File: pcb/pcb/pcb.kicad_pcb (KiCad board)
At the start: 2 copper layers, 58.4 x 44.4 mm, 27 parts, among them J1 UART, J2 Barrel_Jack, J3 Stepper, SW1 RESET, SW2 FLASH, U1 ESP32-WROOM-32, U2 TSR_1-2433

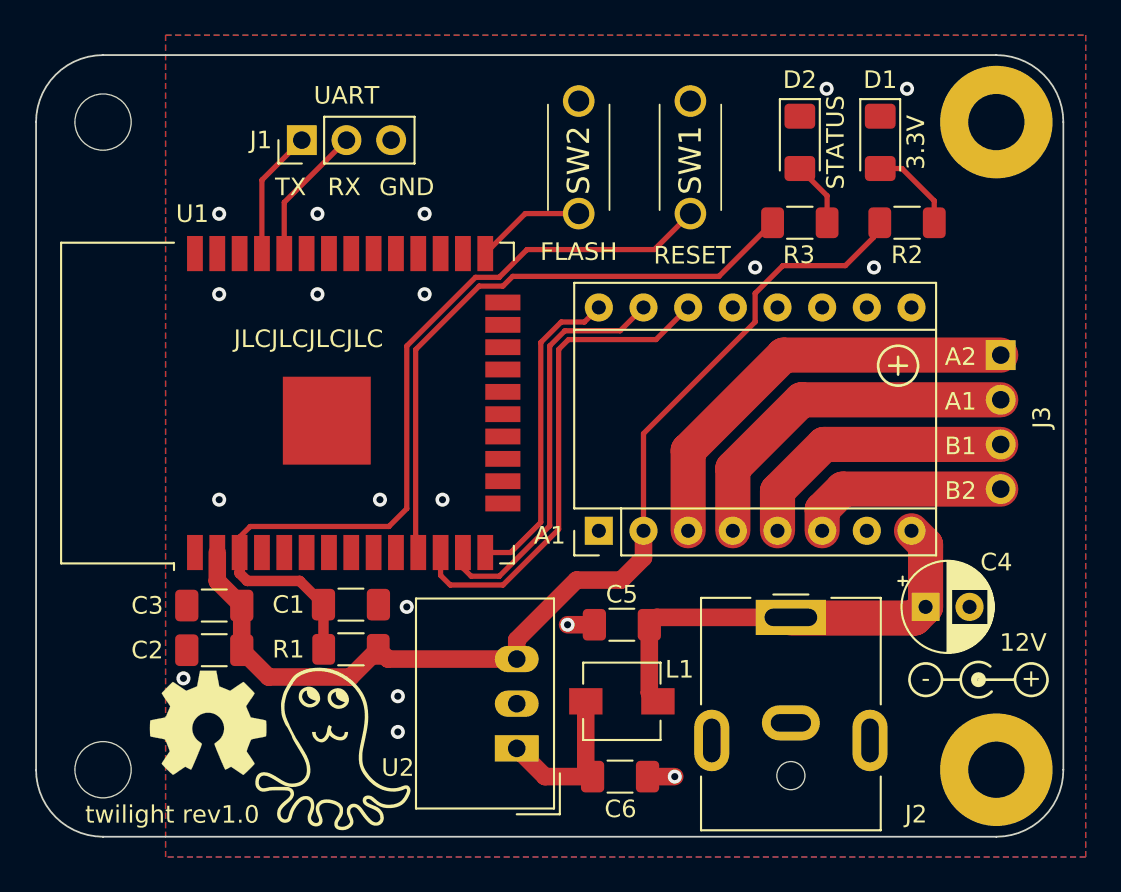
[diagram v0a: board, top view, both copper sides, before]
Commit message: Update pcb to fix bugs
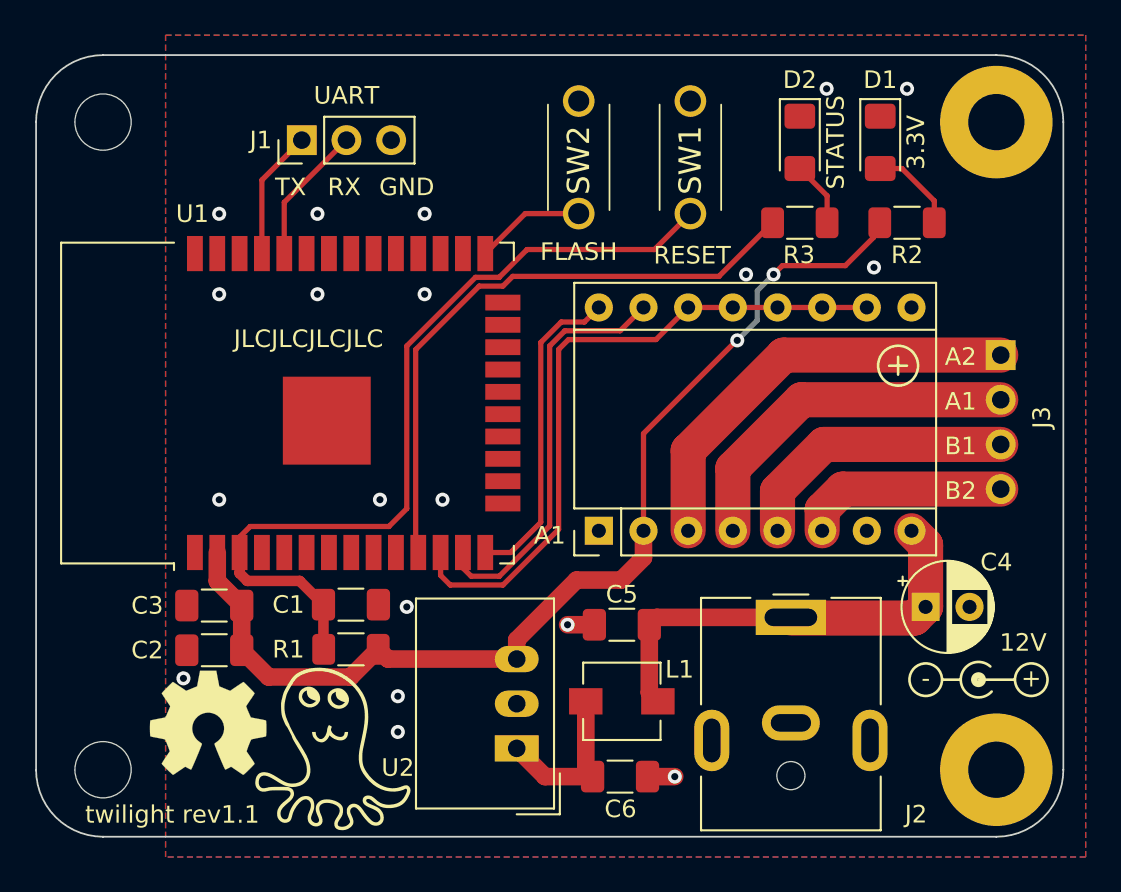
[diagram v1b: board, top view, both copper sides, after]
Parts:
- R2, R3: value 650 -> 680
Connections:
- A1 pad 10: unconnected-(A1-Pad10) -> /SLP
- A1 pad 11: unconnected-(A1-Pad11) -> /SLP
- A1 pad 12: unconnected-(A1-Pad12) -> /SLP
- A1 pad 13: unconnected-(A1-Pad13) -> /SLP
- U1 pad 39: (no net) -> GND
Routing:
- net /SLP: track 28.1 -> 38.3 mm
- net +3V3: track 59.7 -> 59.8 mm, vias 0 -> 2
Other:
- board text added: "twilight rev1.1"
- board text removed: "twilight rev1.0"

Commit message: Optimise routing
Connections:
- A1 pad 10: /SLP -> +3V3
- A1 pad 11: /SLP -> +3V3
- A1 pad 12: /SLP -> +3V3
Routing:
- net /SLP: track 38.3 -> 30.7 mm
- net +3V3: track 59.8 -> 66.2 mm, vias 2 -> 0
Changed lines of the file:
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@@
       (net 4 "unconnected-(A1-Pad9)") (pinfunction "~{EN}") (pintype "input"))
     (pad "10" thru_hole oval (at 12.7 15.24 90) (size 1.6 1.6) (drill 0.8) (layers *.Cu *.Mask)
-      (net 9 "/SLP") (pinfunction "M0") (pintype "input"))
+      (net 3 "+3V3") (pinfunction "M0") (pintype "input"))
     (pad "11" thru_hole oval (at 12.7 12.7 90) (size 1.6 1.6) (drill 0.8) (layers *.Cu *.Mask)
-      (net 9 "/SLP") (pinfunction "M1") (pintype "input"))
+      (net 3 "+3V3") (pinfunction "M1") (pintype "input"))
     (pad "12" thru_hole oval (at 12.7 10.16 90) (size 1.6 1.6) (drill 0.8) (layers *.Cu *.Mask)
-      (net 9 "/SLP") (pinfunction "M2") (pintype "input"))
+      (net 3 "+3V3") (pinfunction "M2") (pintype "input"))
     (pad "13" thru_hole oval (at 12.7 7.62 90) (size 1.6 1.6) (drill 0.8) (layers *.Cu *.Mask)
       (net 9 "/SLP") (pinfunction "~{RST}") (pintype "input"))
@@
   (segment (start 110.744 73.66) (end 108.204 73.66) (width 1) (layer "F.Cu") (net 3))
   (segment (start 90.69082 79.17152) (end 89.1671 77.6478) (width 1) (layer "F.Cu") (net 3))
+  (segment (start 118.596 57.528) (end 118.596 56.778) (width 0.3) (layer "F.Cu") (net 3))
+  (segment (start 118.346 59.236) (end 119.426 58.156) (width 0.3) (layer "F.Cu") (net 3))
   (segment (start 89.1671 77.6478) (end 89.1671 75.1078) (width 1) (layer "F.Cu") (net 3))
-  (segment (start 123.4948 55.7784) (end 125.096786 54.176414) (width 0.3) (layer "F.Cu") (net 3))
   (segment (start 96.927 77.597) (end 97.4799 78.1499) (width 1) (layer "F.Cu") (net 3))
-  (segment (start 125.096786 54.176414) (end 125.096786 53.693213) (width 0.3) (layer "F.Cu") (net 3))
-  (segment (start 117.346 60.028) (end 117.3148 60.028) (width 0.3) (layer "F.Cu") (net 3))
-  (segment (start 117.3148 60.028) (end 112.014 65.3288) (width 0.3) (layer "F.Cu") (net 3))
+  (segment (start 119.426 58.156) (end 119.634 58.156) (width 0.3) (layer "F.Cu") (net 3))
+  (segment (start 119.634 58.156) (end 119.224 58.156) (width 0.3) (layer "F.Cu") (net 3))
+  (segment (start 118.346 60.028) (end 118.346 59.236) (width 0.3) (layer "F.Cu") (net 3))
+  (segment (start 112.014 66.36) (end 118.346 60.028) (width 0.3) (layer "F.Cu") (net 3))
   (segment (start 104.8065 77.0575) (end 104.8065 78.1499) (width 1) (layer "F.Cu") (net 3))
-  (segment (start 119.909762 55.7784) (end 123.4948 55.7784) (width 0.3) (layer "F.Cu") (net 3))
   (segment (start 87.7754 73.7161) (end 87.7754 72.0922) (width 1) (layer "F.Cu") (net 3))
+  (segment (start 118.596 56.778) (end 119.5956 55.7784) (width 0.3) (layer "F.Cu") (net 3))
   (segment (start 96.927 77.597) (end 95.35248 79.17152) (width 1) (layer "F.Cu") (net 3))
+  (segment (start 122.174 58.156) (end 124.714 58.156) (width 0.3) (layer "F.Cu") (net 3))
   (segment (start 112.014 70.856) (end 112.014 72.39) (width 1) (layer "F.Cu") (net 3))
+  (segment (start 112.014 70.856) (end 112.014 66.36) (width 0.3) (layer "F.Cu") (net 3))
   (segment (start 97.4799 78.1499) (end 104.8065 78.1499) (width 1) (layer "F.Cu") (net 3))
   (segment (start 95.35248 79.17152) (end 90.69082 79.17152) (width 1) (layer "F.Cu") (net 3))
+  (segment (start 119.634 58.156) (end 122.174 58.156) (width 0.3) (layer "F.Cu") (net 3))
   (segment (start 108.204 73.66) (end 104.8065 77.0575) (width 1) (layer "F.Cu") (net 3))
-  (segment (start 112.014 65.3288) (end 112.014 70.856) (width 0.3) (layer "F.Cu") (net 3))
   (segment (start 112.014 72.39) (end 110.744 73.66) (width 1) (layer "F.Cu") (net 3))
-  (segment (start 119.410162 56.278) (end 119.909762 55.7784) (width 0.3) (layer "F.Cu") (net 3))
+  (segment (start 119.5956 55.7784) (end 123.4948 55.7784) (width 0.3) (layer "F.Cu") (net 3))
+  (segment (start 123.4948 55.7784) (end 125.096786 54.176414) (width 0.3) (layer "F.Cu") (net 3))
+  (segment (start 125.096786 54.176414) (end 125.096786 53.693213) (width 0.3) (layer "F.Cu") (net 3))
+  (segment (start 119.224 58.156) (end 118.596 57.528) (width 0.3) (layer "F.Cu") (net 3))
   (segment (start 89.1671 75.1078) (end 87.7754 73.7161) (width 1) (layer "F.Cu") (net 3))
-  (via (at 117.346 60.028) (size 0.8) (drill 0.4) (layers "F.Cu" "B.Cu") (net 3))
-  (via (at 119.410162 56.278) (size 0.8) (drill 0.4) (layers "F.Cu" "B.Cu") (net 3))
-  (segment (start 118.484489 57.203673) (end 118.484489 58.889511) (width 0.3) (layer "B.Cu") (net 3))
-  (segment (start 119.410162 56.278) (end 118.484489 57.203673) (width 0.3) (layer "B.Cu") (net 3))
-  (segment (start 118.484489 58.889511) (end 117.346 60.028) (width 0.3) (layer "B.Cu") (net 3))
   (segment (start 114.554 70.856) (end 114.554 66.294) (width 2) (layer "F.Cu") (net 5))
   (segment (start 114.554 66.294) (end 119.9821 60.8659) (width 2) (layer "F.Cu") (net 5))
@@
   (segment (start 104.021818 73.941231) (end 107.188 70.775049) (width 0.3) (layer "F.Cu") (net 9))
   (segment (start 107.188 70.775049) (end 107.188 60.544056) (width 0.3) (layer "F.Cu") (net 9))
-  (segment (start 122.174 58.156) (end 124.714 58.156) (width 0.3) (layer "F.Cu") (net 9))
-  (segment (start 117.094 58.156) (end 119.634 58.156) (width 0.3) (layer "F.Cu") (net 9))
-  (segment (start 119.634 58.156) (end 122.174 58.156) (width 0.3) (layer "F.Cu") (net 9))
   (segment (start 100.4754 73.3922) (end 101.024431 73.941231) (width 0.3) (layer "F.Cu") (net 9))
   (segment (start 114.554 58.156) (end 117.094 58.156) (width 0.3) (layer "F.Cu") (net 9))
